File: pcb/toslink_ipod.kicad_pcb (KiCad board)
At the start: 2 copper layers, 16.3 x 17.8 mm, 20 parts, among them U1 WM8804, Y1 22.5792MHz

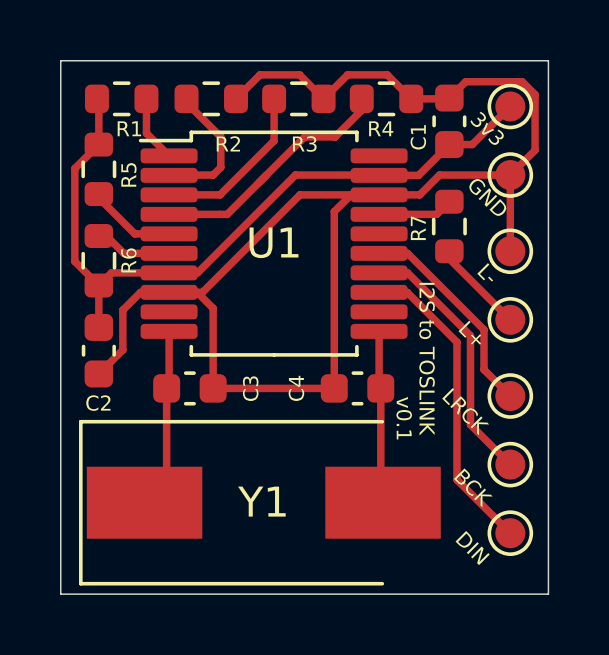
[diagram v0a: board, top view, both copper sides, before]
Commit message: Flip C1 for shorter traces
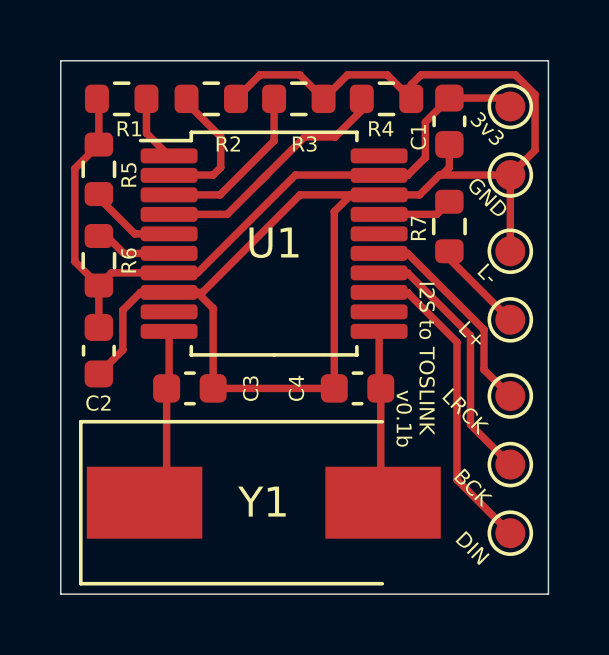
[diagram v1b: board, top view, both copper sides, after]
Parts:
- turned C1 to 270 degrees
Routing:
- net GND: track 50.5 -> 52.1 mm
- net +3V3: track 25.2 -> 26.1 mm
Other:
- board text added: "v0.1b"
- board text removed: "v0.1"
